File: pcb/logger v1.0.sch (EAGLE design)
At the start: 33 parts, among them J1 MICRO-SDCARD-CONNECTOR-330006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, K1 RESET, U1 DS1307ZN-1900100P1, U2 CJ1117-3.3-1310190P1, U3 74VHCT125PW, X1 32.768KHZ

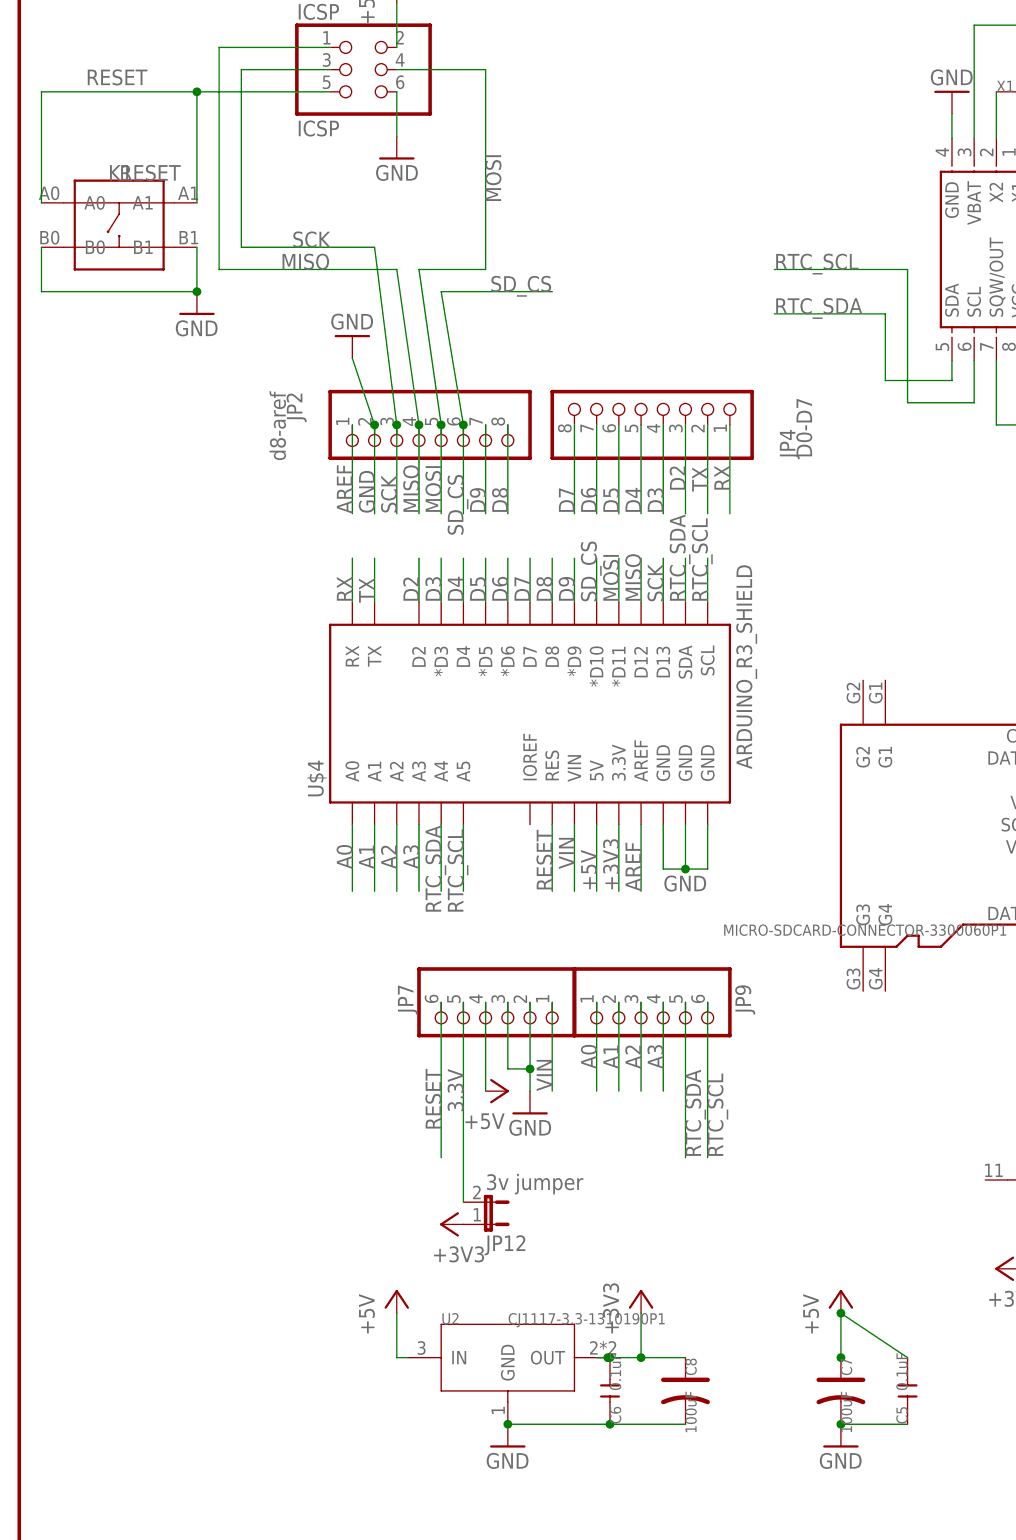
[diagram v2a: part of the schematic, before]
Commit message: Changed and rerouted to match OPL availability
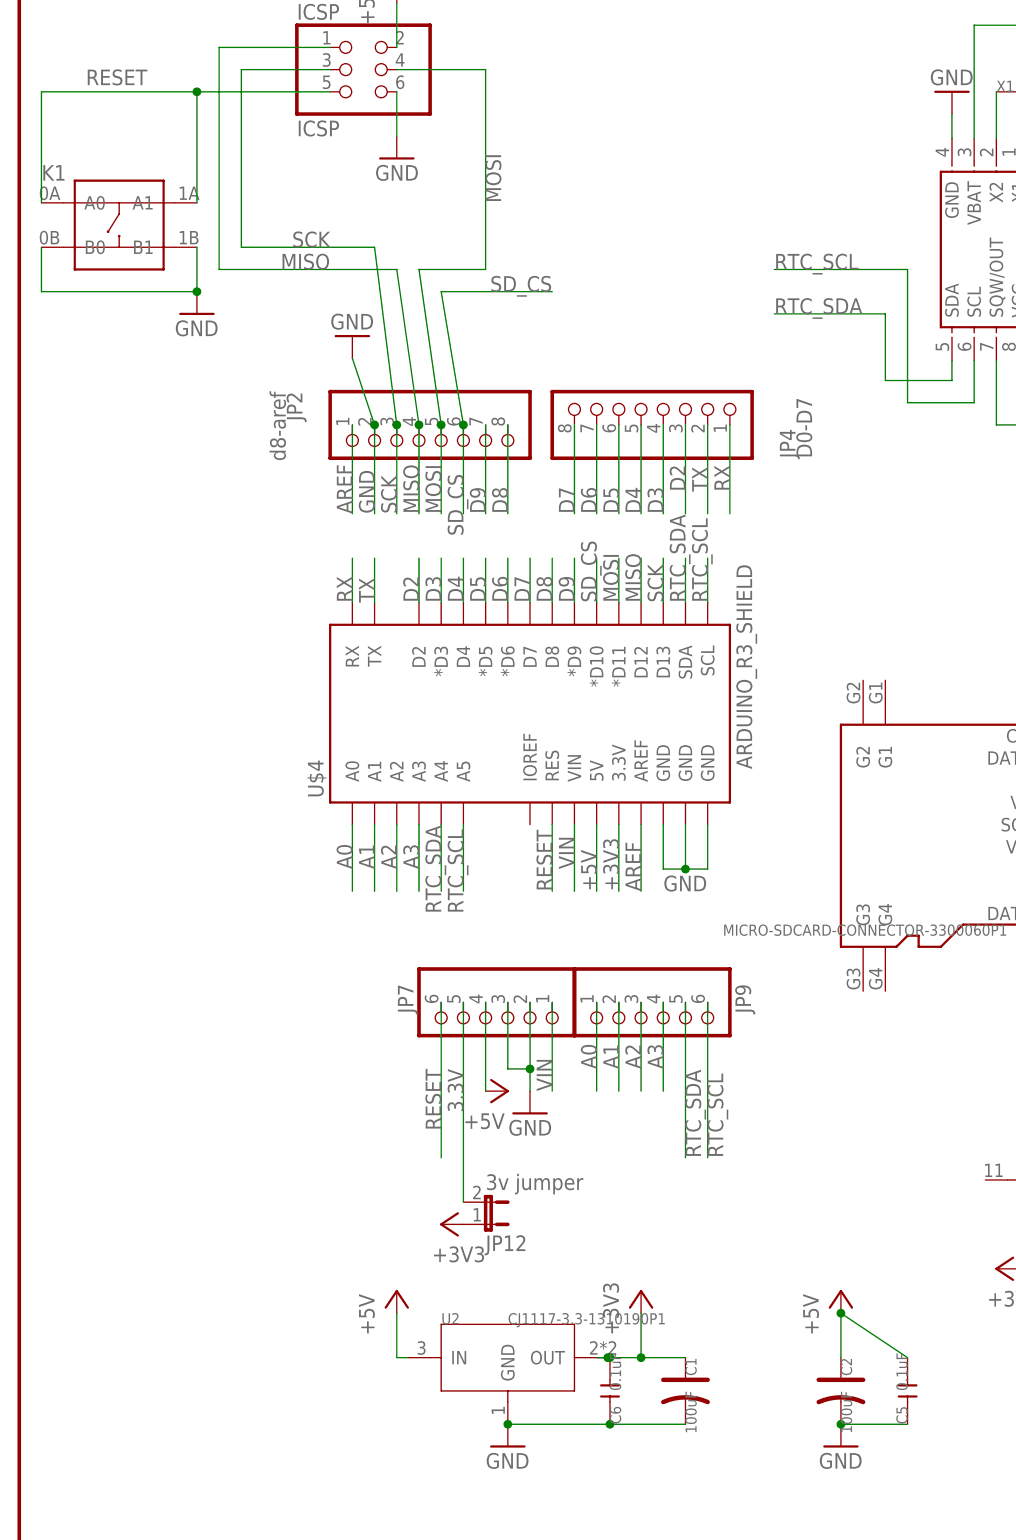
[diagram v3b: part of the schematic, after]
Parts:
- removed C7, C8: 100uF, Discrete:CAP-ELECTRO-A
- added C1, C2: 100uF, Discrete:CAP-ELECTRO-B
- K1: value RESET -> (none); device Discrete:BUTTON-4P-3.3X3.3 -> Discrete:BUTTON-4P-6X6-SMD
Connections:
- net +3V3: now also C1.+; no longer C8.+
- net +5V: now also C2.+; no longer C7.+
- net GND: now also C1.-, C2.-; no longer C7.-, C8.-
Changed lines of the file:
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@@
 <part name="C5" library="Discrete" deviceset="C*" device="-0603" value="0.1uF"/>
 <part name="C6" library="Discrete" deviceset="C*" device="-0603" value="0.1uF"/>
-<part name="C7" library="Discrete" deviceset="CAP*" device="-ELECTRO-A" value="100uF"/>
-<part name="C8" library="Discrete" deviceset="CAP*" device="-ELECTRO-A" value="100uF"/>
 <part name="U1" library="OPL" deviceset="DS1307ZN" device="-1900100P1"/>
 <part name="U2" library="OPL" deviceset="CJ1117-3.3" device="-1310190P1"/>
 <part name="U3" library="IC" deviceset="74V*125" device="PW" technology="HCT"/>
-<part name="K1" library="Discrete" deviceset="BUTTON-4P" device="-3.3X3.3" value="RESET"/>
 <part name="BAT1" library="Connector" deviceset="BAT-HOLDER" device="-SMD-1220" value="CR1220"/>
 <part name="GND9" library="supply1" deviceset="GND" device=""/>
@@
 <part name="R2" library="Discrete" deviceset="R*" device="-0603" value="1k"/>
 <part name="D4" library="Discrete" deviceset="LED*" device="'0603'" value="POWER"/>
+<part name="C1" library="Discrete" deviceset="CAP*" device="-ELECTRO-B" value="100uF"/>
+<part name="C2" library="Discrete" deviceset="CAP*" device="-ELECTRO-B" value="100uF"/>
+<part name="K1" library="Discrete" deviceset="BUTTON-4P" device="-6X6-SMD"/>
 </parts>
 <sheets>
@@
 <instance part="C5" gate="C" x="101.6" y="19.05" rot="R90"/>
 <instance part="C6" gate="C" x="67.564" y="19.05" rot="MR90"/>
-<instance part="C7" gate="C" x="93.98" y="19.05" rot="R270"/>
-<instance part="C8" gate="C" x="76.2" y="19.05" rot="R270"/>
 <instance part="U1" gate="U" x="110.49" y="149.606" rot="R270"/>
 <instance part="U2" gate="U" x="55.88" y="22.86"/>
@@
 <instance part="U3" gate="C" x="165.1" y="68.58" rot="MR0"/>
 <instance part="U3" gate="D" x="119.38" y="43.18" rot="MR0"/>
-<instance part="K1" gate="G$1" x="11.43" y="152.4" smashed="yes">
-<attribute name="NAME" x="10.16" y="157.48" size="1.778" layer="95"/>
-<attribute name="VALUE" x="11.43" y="157.48" size="1.778" layer="96"/>
-</instance>
 <instance part="BAT1" gate="G$1" x="134.62" y="135.382" rot="R90"/>
 <instance part="GND9" gate="1" x="214.63" y="170.18" rot="R90"/>
@@
 <instance part="R2" gate="R" x="195.58" y="160.02"/>
 <instance part="D4" gate="LED" x="205.74" y="160.02"/>
+<instance part="C1" gate="C" x="76.2" y="19.05" rot="R270"/>
+<instance part="C2" gate="C" x="93.98" y="19.05" rot="R270"/>
+<instance part="K1" gate="G$1" x="11.43" y="152.4"/>
 </instances>
 <busses>
@@
 <junction x="93.98" y="27.94"/>
 <pinref part="P+4" gate="1" pin="+5V"/>
-<pinref part="C7" gate="C" pin="+"/>
-<junction x="93.98" y="22.86"/>
 <pinref part="C5" gate="C" pin="2"/>
+<pinref part="C2" gate="C" pin="+"/>
 </segment>
 <segment>
@@
 <wire x1="101.6" y1="15.24" x2="93.98" y2="15.24" width="0.1524" layer="91"/>
 <pinref part="GND8" gate="1" pin="GND"/>
-<pinref part="C7" gate="C" pin="-"/>
+<pinref part="C5" gate="C" pin="1"/>
+<pinref part="C2" gate="C" pin="-"/>
 <junction x="93.98" y="15.24"/>
-<pinref part="C5" gate="C" pin="1"/>
 </segment>
 <segment>
@@
 <wire x1="67.564" y1="15.24" x2="76.2" y2="15.24" width="0.1524" layer="91"/>
 <junction x="67.564" y="15.24"/>
-<pinref part="C8" gate="C" pin="-"/>
 <pinref part="U2" gate="U" pin="GND"/>
 <junction x="55.88" y="15.24"/>
+<pinref part="C1" gate="C" pin="-"/>
 </segment>
 <segment>
@@
 <wire x1="20.32" y1="144.78" x2="2.54" y2="144.78" width="0.1524" layer="91"/>
 <wire x1="2.54" y1="144.78" x2="2.54" y2="149.86" width="0.1524" layer="91"/>
-<pinref part="K1" gate="G$1" pin="B0"/>
 <wire x1="20.32" y1="144.78" x2="20.32" y2="149.86" width="0.1524" layer="91"/>
 <junction x="20.32" y="144.78"/>
+<pinref part="K1" gate="G$1" pin="B0"/>
 <pinref part="K1" gate="G$1" pin="B1"/>
 </segment>
@@
 <pinref part="C6" gate="C" pin="2"/>
 <junction x="67.564" y="22.86"/>
-<pinref part="C8" gate="C" pin="+"/>
 <pinref part="U2" gate="U" pin="OUT"/>
 <junction x="67.31" y="22.86"/>
-</segment>
-<segment>
+<pinref part="C1" gate="C" pin="+"/>
+</segment>
+<segment>
